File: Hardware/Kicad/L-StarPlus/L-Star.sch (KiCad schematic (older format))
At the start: 51 parts, among them IC1 24LC512, IC2 AS6C1008-55PCN, IC3 WDC 65C02, IC4 P8X32A, IC5 LM1086-5.0, IC6 LM1086-3.3, P1 PROP PLUG, P2 EXPANSION, P3 PS/2 KBD, P4 RESET, P5 RESET6502, P6 VIDEO OUT, P7 7-15V 1-1.5A IN, SW1 RESET, SW2 RESET6502, SW3 PWR SWITCH, U1 OSHW Logo, U2 Mount hole, U3 Mount hole, U4 Mount hole, X1 5MHz

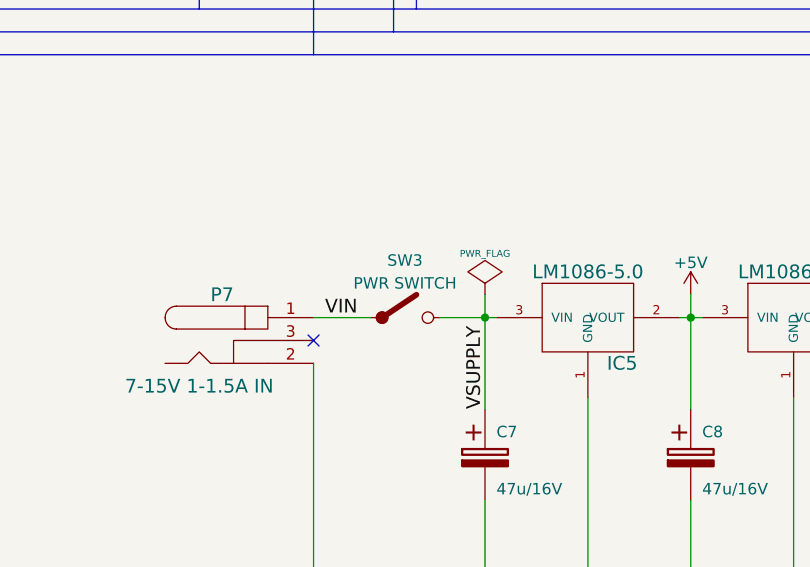
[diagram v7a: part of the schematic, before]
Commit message: Added a slider switch to the PCB, and reduced board size
The switch that I selected from Mouser didn't quite fit on the board with the components arranged the way they were, so I had to move a lot of stuff around. As a matter of fact, I had to move a LOT of stuff around and decided to try and make the board smaller. I would have liked to get the size under 100mm x 80mm (1/2 Eurocard) but didn't quite make it. Still, the new board is 13% smaller than the old size.
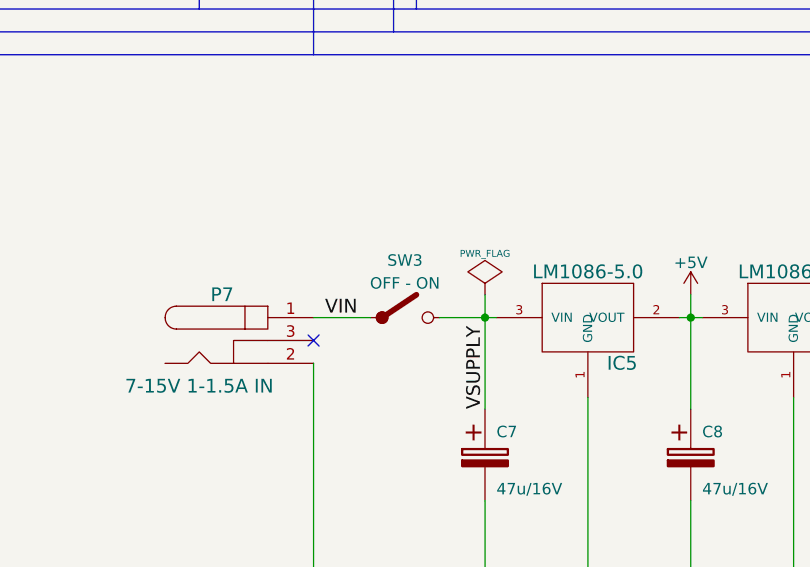
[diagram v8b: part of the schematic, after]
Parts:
- SW3: value PWR SWITCH -> OFF - ON; footprint 00Jac:00JG-SHORTED_Pin_Header_Straight_1x02 -> 00Jac:00JG-NKK_CS12ANW03
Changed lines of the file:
@@
 Sheet 1 1
 Title "L-Star Simplified Software-Defined 6502 Computer Kit"
-Date "2016-05-08"
+Date "2016-05-15"
 Rev "2"
 Comp "(C) 2016 Jac Goudsmit"
@@
 P 4850 8700
 F 0 "SW3" H 4850 8950 50  0000 C CNN
-F 1 "PWR SWITCH" H 4850 8850 50  0000 C CNN
-F 2 "00Jac:00JG-SHORTED_Pin_Header_Straight_1x02" H 4850 8850 50  0001 C CNN
+F 1 "OFF - ON" H 4850 8850 50  0000 C CNN
+F 2 "00Jac:00JG-NKK_CS12ANW03" H 4850 8850 50  0001 C CNN
 F 3 "" H 4850 8700 60  0000 C CNN
 	1    4850 8700
